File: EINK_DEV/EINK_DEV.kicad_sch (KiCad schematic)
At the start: 77 parts, among them J1 FPC, J2 USB_B_Micro, J3 Conn_01x02, J4 Conn_01x03, J5 Conn_ARM_SWD_TagConnect_TC2030, J6 UART, J7 Conn_Coaxial, J8 GPIO_Header_Dev, Q1 NMOS, SW1 SW_Push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

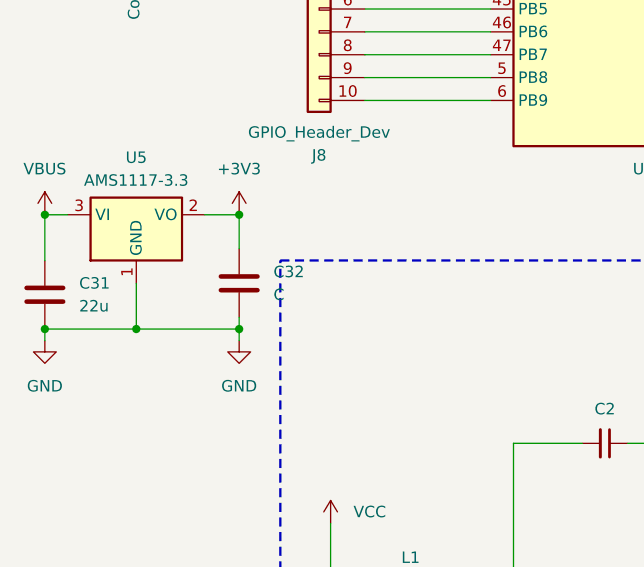
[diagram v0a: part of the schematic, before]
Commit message: Assign value to capacitor C32
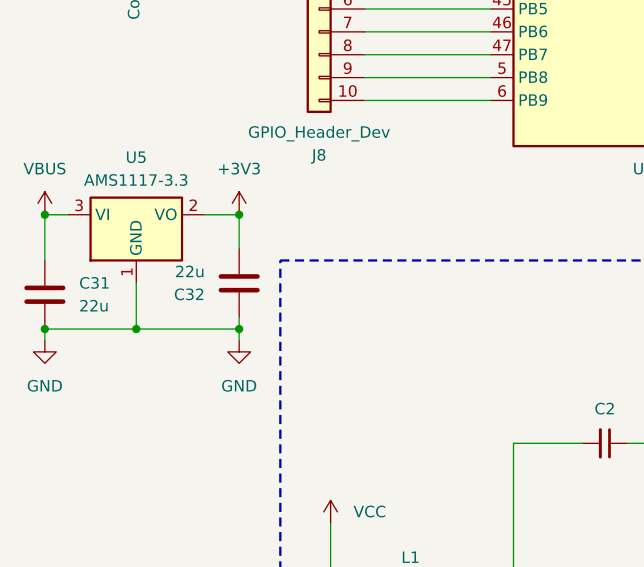
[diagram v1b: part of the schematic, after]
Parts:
- C32: value C -> 22u
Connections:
- net +3V3: now also C32.2; no longer C32.1
- net GND: now also C32.1; no longer C32.2
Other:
- moved on the sheet: C32
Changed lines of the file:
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@@
 	(symbol
 		(lib_id "Device:C")
-		(at 39.37 129.54 0)
+		(at 39.37 129.54 180)
 		(unit 1)
 		(exclude_from_sim no)
@@
 		(on_board yes)
 		(dnp no)
-		(fields_autoplaced yes)
 		(property "Reference" "C32"
-			(at 43.18 128.2699 0)
+			(at 35.56 130.8101 0)
 			(effects
 				(font
@@
 			)
 		)
-		(property "Value" "C"
-			(at 43.18 130.8099 0)
+		(property "Value" "22u"
+			(at 35.56 128.2701 0)
 			(effects
 				(font
@@
 		)
 		(property "Footprint" ""
-			(at 40.3352 133.35 0)
+			(at 38.4048 125.73 0)
 			(effects
 				(font

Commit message: Commit
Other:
- note added: "Regulator"
- moved on the sheet: C1, C2, C3, C31, C32, C4, D1, D2, D3, L1, Q1, U5

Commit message: Poprawka Zasilania
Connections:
- net +BATT: now also C31.1, U5.3 (VI)
- net VBUS: no longer C31.1, U5.3 (VI)
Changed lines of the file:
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@@
 	)
 	(junction
-		(at 214.63 64.77)
-		(diameter 0)
-		(color 0 0 0 0)
-	)
-	(junction
 		(at 218.44 132.08)
 		(diameter 0)
@@
 	)
 	(junction
+		(at 214.63 64.77)
+		(diameter 0)
+		(color 0 0 0 0)
+	)
+	(junction
 		(at 102.87 151.13)
 		(diameter 0)
@@
 	(wire
 		(pts
-			(xy 214.63 64.77) (xy 227.33 64.77)
+			(xy 209.55 64.77) (xy 214.63 64.77)
 		)
 		(stroke
@@
 	(wire
 		(pts
-			(xy 218.44 152.4) (xy 218.44 162.56)
+			(xy 218.44 152.4) (xy 218.44 157.48)
 		)
 		(stroke
@@
 	(wire
 		(pts
-			(xy 209.55 64.77) (xy 214.63 64.77)
-		)
-		(stroke
-			(width 0)
-			(type default)
-		)
-	)
-	(wire
-		(pts
 			(xy 154.94 184.15) (xy 158.75 184.15)
 		)
@@
 	(wire
 		(pts
+			(xy 214.63 64.77) (xy 227.33 64.77)
+		)
+		(stroke
+			(width 0)
+			(type default)
+		)
+	)
+	(wire
+		(pts
 			(xy 72.39 27.94) (xy 80.01 27.94)
 		)
@@
 	(symbol
 		(lib_id "power:GND")
-		(at 214.63 64.77 0)
-		(unit 1)
-		(exclude_from_sim no)
-		(in_bom yes)
-		(on_board yes)
-		(dnp no)
-		(fields_autoplaced yes)
-		(property "Reference" "#PWR022"
-			(at 214.63 71.12 0)
-			(effects
-				(font
-					(size 1.27 1.27)
-				)
-				(hide yes)
-			)
-		)
-		(property "Value" "BAT PRZYŁ"
-			(at 214.63 69.85 0)
-			(effects
-				(font
-					(size 1.27 1.27)
-				)
-			)
-		)
-		(property "Footprint" ""
-			(at 214.63 64.77 0)
-			(effects
-				(font
-					(size 1.27 1.27)
-				)
-				(hide yes)
-			)
-		)
-		(property "Datasheet" ""
-			(at 214.63 64.77 0)
-			(effects
-				(font
-					(size 1.27 1.27)
-				)
-				(hide yes)
-			)
-		)
-		(property "Description" "Power symbol creates a global label with name \"GND\" , ground"
-			(at 214.63 64.77 0)
-			(effects
-				(font
-					(size 1.27 1.27)
-				)
-				(hide yes)
-			)
-		)
-		(pin "1"
-		)
-		(instances
-			(project "EINK_DEV"
-				(path "/21ffd272-94a2-4b6a-9954-5d1217824b1f"
-					(reference "#PWR022")
-					(unit 1)
-				)
-			)
-		)
-	)
-	(symbol
-		(lib_id "power:GND")
 		(at 214.63 110.49 0)
 		(unit 1)
@@
 	(symbol
 		(lib_id "power:GND")
-		(at 218.44 162.56 0)
+		(at 218.44 157.48 0)
 		(unit 1)
 		(exclude_from_sim no)
@@
 		(fields_autoplaced yes)
 		(property "Reference" "#PWR020"
-			(at 218.44 168.91 0)
+			(at 218.44 163.83 0)
 			(effects
 				(font
@@
 		)
 		(property "Value" "GND"
-			(at 218.44 167.64 0)
+			(at 218.44 162.56 0)
 			(effects
 				(font
@@
 		)
 		(property "Footprint" ""
-			(at 218.44 162.56 0)
+			(at 218.44 157.48 0)
 			(effects
 				(font
@@
 		)
 		(property "Datasheet" ""
-			(at 218.44 162.56 0)
+			(at 218.44 157.48 0)
 			(effects
 				(font
@@
 		)
 		(property "Description" "Power symbol creates a global label with name \"GND\" , ground"
-			(at 218.44 162.56 0)
+			(at 218.44 157.48 0)
 			(effects
 				(font
@@
 	)
 	(symbol
+		(lib_id "power:VBUS")
+		(at 214.63 64.77 180)
+		(unit 1)
+		(exclude_from_sim no)
+		(in_bom yes)
+		(on_board yes)
+		(dnp no)
+		(property "Reference" "#PWR052"
+			(at 214.63 60.96 0)
+			(effects
+				(font
+					(size 1.27 1.27)
+				)
+				(hide yes)
+			)
+		)
+		(property "Value" "OUT+"
+			(at 216.662 70.104 0)
+			(effects
+				(font
+					(size 1.27 1.27)
+				)
+				(justify left)
+			)
+		)
+		(property "Footprint" ""
+			(at 214.63 64.77 0)
+			(effects
+				(font
+					(size 1.27 1.27)
+				)
+				(hide yes)
+			)
+		)
+		(property "Datasheet" ""
+			(at 214.63 64.77 0)
+			(effects
+				(font
+					(size 1.27 1.27)
+				)
+				(hide yes)
+			)
+		)
+		(property "Description" "Power symbol creates a global label with name \"VBUS\""
+			(at 214.63 64.77 0)
+			(effects
+				(font
+					(size 1.27 1.27)
+				)
+				(hide yes)
+			)
+		)
+		(pin "1"
+		)
+		(instances
+			(project "EINK_DEV"
+				(path "/21ffd272-94a2-4b6a-9954-5d1217824b1f"
+					(reference "#PWR052")
+					(unit 1)
+				)
+			)
+		)
+	)
+	(symbol
 		(lib_id "power:VCC")
 		(at 124.46 156.21 90)
@@
 		(on_board yes)
 		(dnp no)
-		(fields_autoplaced yes)
 		(property "Reference" "#PWR047"
 			(at 17.78 139.7 0)
@@
 			)
 		)
-		(property "Value" "VBUS"
-			(at 17.78 130.81 0)
+		(property "Value" "OUT+"
+			(at 15.748 130.556 0)
 			(effects
 				(font
 					(size 1.27 1.27)
 				)
+				(justify left)
 			)
 		)
@@
 	)
 	(symbol
-		(lib_id "power:GND")
-		(at 189.23 137.16 0)
-		(unit 1)
-		(exclude_from_sim no)
-		(in_bom yes)
-		(on_board yes)
-		(dnp no)
-		(fields_autoplaced yes)
-		(property "Reference" "#PWR024"
-			(at 189.23 143.51 0)
-			(effects
-				(font
-					(size 1.27 1.27)
-				)
-				(hide yes)
-			)
-		)
-		(property "Value" "BAT PRZYŁ"
-			(at 189.23 142.24 0)
-			(effects
-				(font
-					(size 1.27 1.27)
-				)
-			)
-		)
-		(property "Footprint" ""
-			(at 189.23 137.16 0)
-			(effects
-				(font
-					(size 1.27 1.27)
-				)
-				(hide yes)
-			)
-		)
-		(property "Datasheet" ""
-			(at 189.23 137.16 0)
-			(effects
-				(font
-					(size 1.27 1.27)
-				)
-				(hide yes)
-			)
-		)
-		(property "Description" "Power symbol creates a global label with name \"GND\" , ground"
-			(at 189.23 137.16 0)
-			(effects
-				(font
-					(size 1.27 1.27)
-				)
-				(hide yes)
-			)
-		)
-		(pin "1"
-		)
-		(instances
-			(project "EINK_DEV"
-				(path "/21ffd272-94a2-4b6a-9954-5d1217824b1f"
-					(reference "#PWR024")
-					(unit 1)
-				)
-			)
-		)
-	)
-	(symbol
 		(lib_id "Device:C")
 		(at 39.37 143.51 180)
@@
 					(unit 1)
 				)
+			)
+		)
+	)
+	(symbol
+		(lib_id "power:VBUS")
+		(at 189.23 137.16 180)
+		(unit 1)
+		(exclude_from_sim no)
+		(in_bom yes)
+		(on_board yes)
+		(dnp no)
+		(property "Reference" "#PWR051"
+			(at 189.23 133.35 0)
+			(effects
+				(font
+					(size 1.27 1.27)
+				)
+				(hide yes)
+			)
+		)
+		(property "Value" "OUT+"
+			(at 191.262 142.494 0)
+			(effects
+				(font
+					(size 1.27 1.27)
+				)
+				(justify left)
+			)
+		)
+		(property "Footprint" ""
+			(at 189.23 137.16 0)
+			(effects
+				(font
+					(size 1.27 1.27)
+				)
+				(hide yes)
+			)
+		)
+		(property "Datasheet" ""
+			(at 189.23 137.16 0)
+			(effects
+				(font
+					(size 1.27 1.27)
+				)
+				(hide yes)
+			)
+		)
+		(property "Description" "Power symbol creates a global label with name \"VBUS\""
+			(at 189.23 137.16 0)
+			(effects
+				(font
+					(size 1.27 1.27)
+				)
+				(hide yes)
+			)
+		)
+		(pin "1"
+		)
+		(instances
+			(project "EINK_DEV"
+				(path "/21ffd272-94a2-4b6a-9954-5d1217824b1f"
+					(reference "#PWR051")
+					(unit 1)
+				)

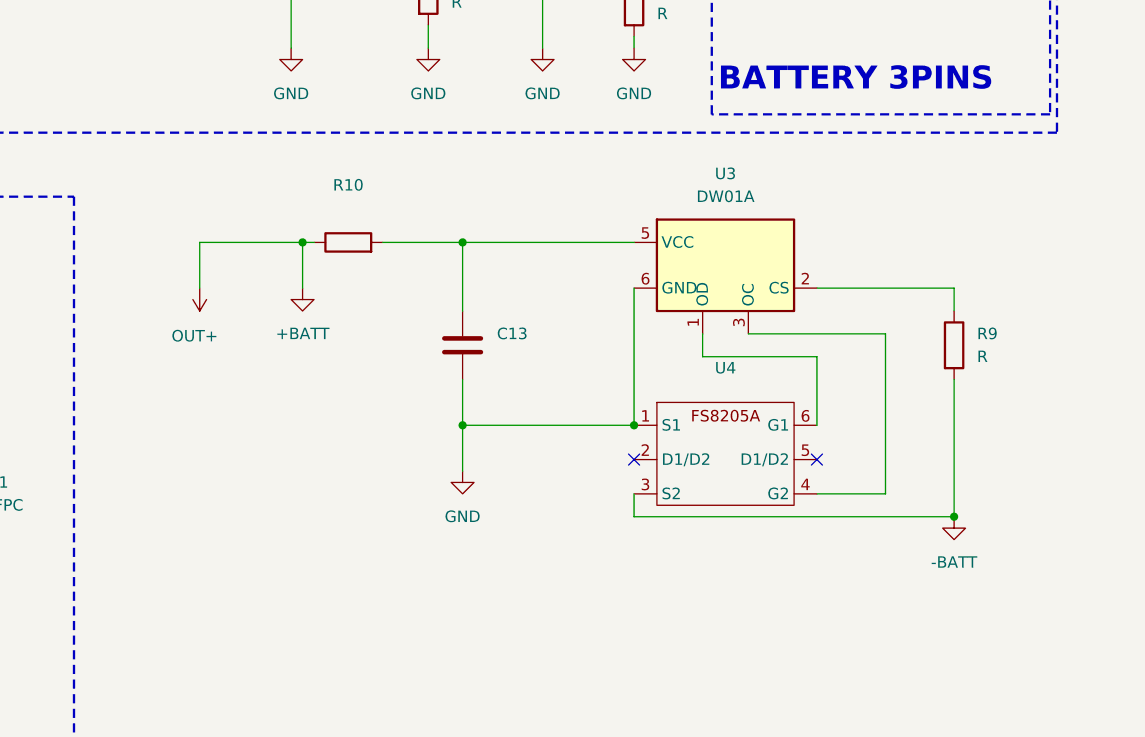
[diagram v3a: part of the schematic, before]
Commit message: Remove charging battery module protection
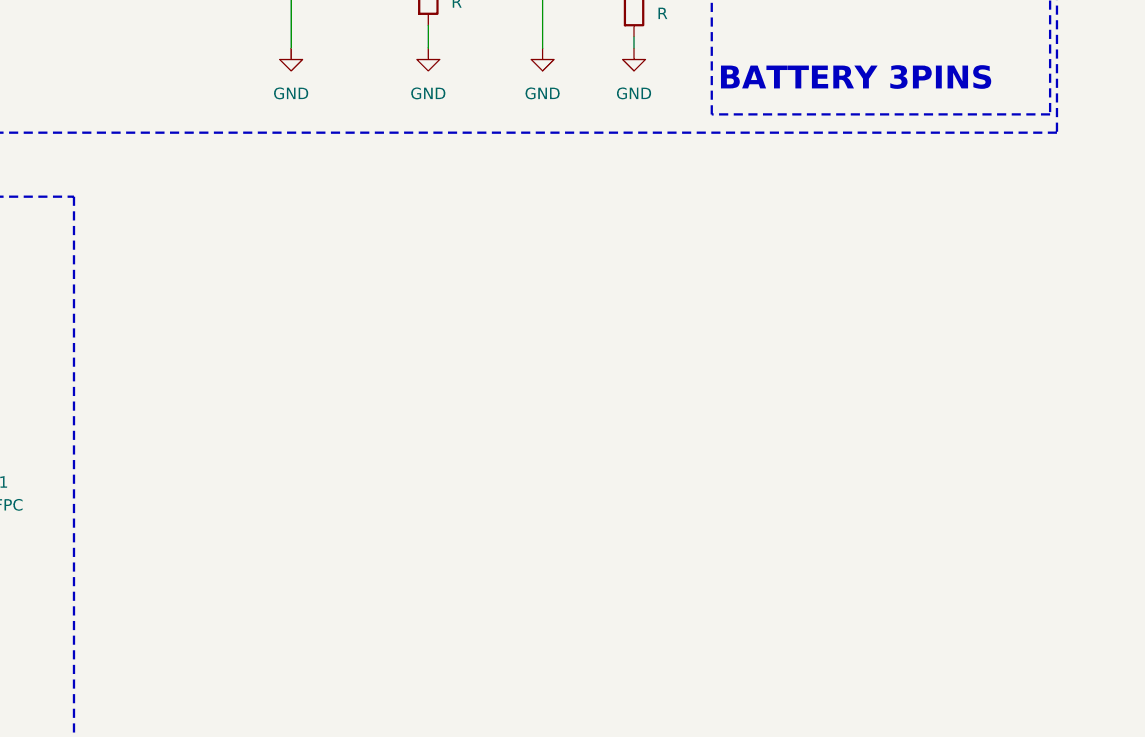
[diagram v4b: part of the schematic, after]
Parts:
- removed C13: ~, symbol Device:C
- removed R10: ~, symbol Device:R
- removed R9: R, symbol Device:R
- removed U3: DW01A, Package_TO_SOT_SMD:SOT-23-6, symbol Battery_Management:DW01A
- removed U4: ~, symbol Battery_Management:FS8205A
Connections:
- net +BATT renamed OUT+
- no-connect marks 7 -> 5

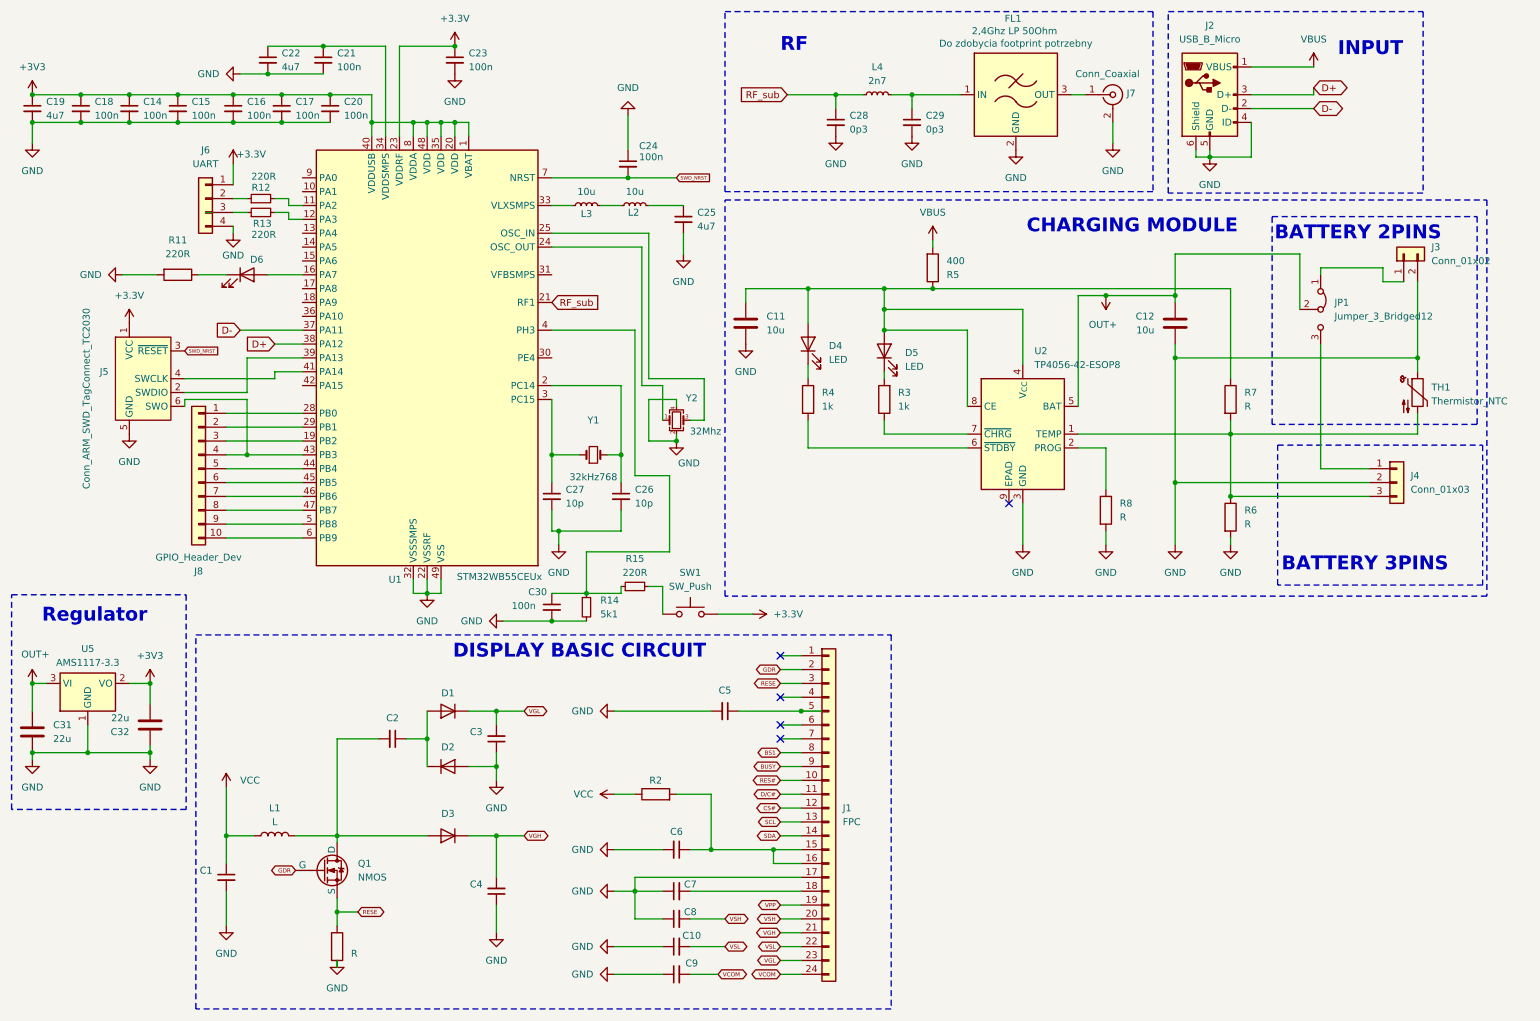
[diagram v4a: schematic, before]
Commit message: Add USB C
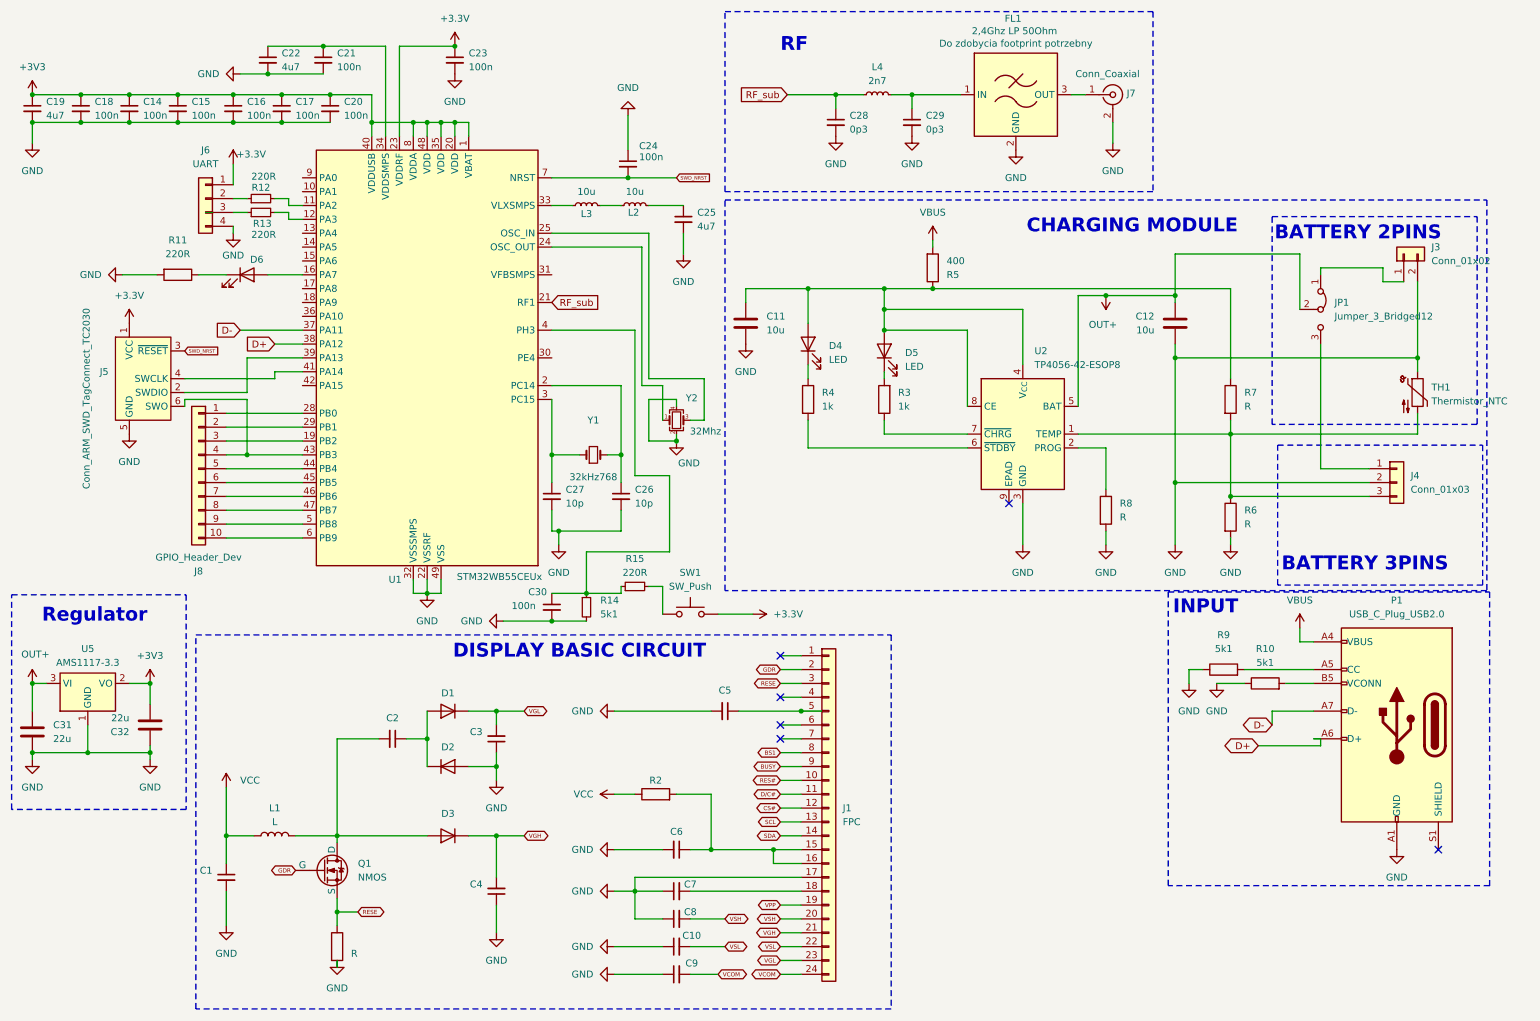
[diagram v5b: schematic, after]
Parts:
- removed J2: USB_B_Micro, symbol Connector:USB_B_Micro
- added P1: USB_C_Plug_USB2.0, symbol Connector:USB_C_Plug_USB2.0
- added R10, R9: 5k1, symbol Device:R
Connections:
- net D+: now also P1.A6 (D+)
- net D-: now also P1.A7 (D-)
- net GND: now also P1.A1 (GND), P1.A12 (GND), P1.B1 (GND), P1.B12 (GND), R10.1, R9.1
- net VBUS: now also P1.A4 (VBUS), P1.A9 (VBUS), P1.B4 (VBUS), P1.B9 (VBUS)
- new net: P1.A5 (CC), R9.2
- new net: P1.B5 (VCONN), R10.2
- no-connect marks 5 -> 6

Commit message: LDO v2
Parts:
- removed U5: AMS1117-3.3, Package_TO_SOT_SMD:SOT-223-3_TabPin2, symbol Regulator_Linear:AMS1117-3.3
- added C33: 0.1u, symbol Device:C
- added U3: MIC5219-3.3YMM, Package_SO:MSOP-8_3x3mm_P0.65mm, symbol Regulator_Linear:MIC5219-3.3YMM
- C31, C32: value 22u -> 10u
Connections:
- net +3V3: now also C32.1, C33.1, U3.3 (OUT); no longer C32.2
- net GND: now also C32.2, C33.2, U3.5 (GND), U3.6 (GND), U3.7 (GND), U3.8 (GND); no longer C32.1
- net OUT+: now also U3.1 (EN), U3.2 (IN)
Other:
- moved on the sheet: C31, C32
